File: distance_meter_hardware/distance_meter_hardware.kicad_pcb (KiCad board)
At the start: 2 copper layers, 62.2 x 53.3 mm, 6 parts, among them J1 PPPC071LFBN-RC, J2 PPPC071LFBN-RC, J3 PPPC141LFBN-RC, J4 PPPC141LFBN-RC, J5 PPPC071LFBN-RC, J6 PPPC071LFBN-RC

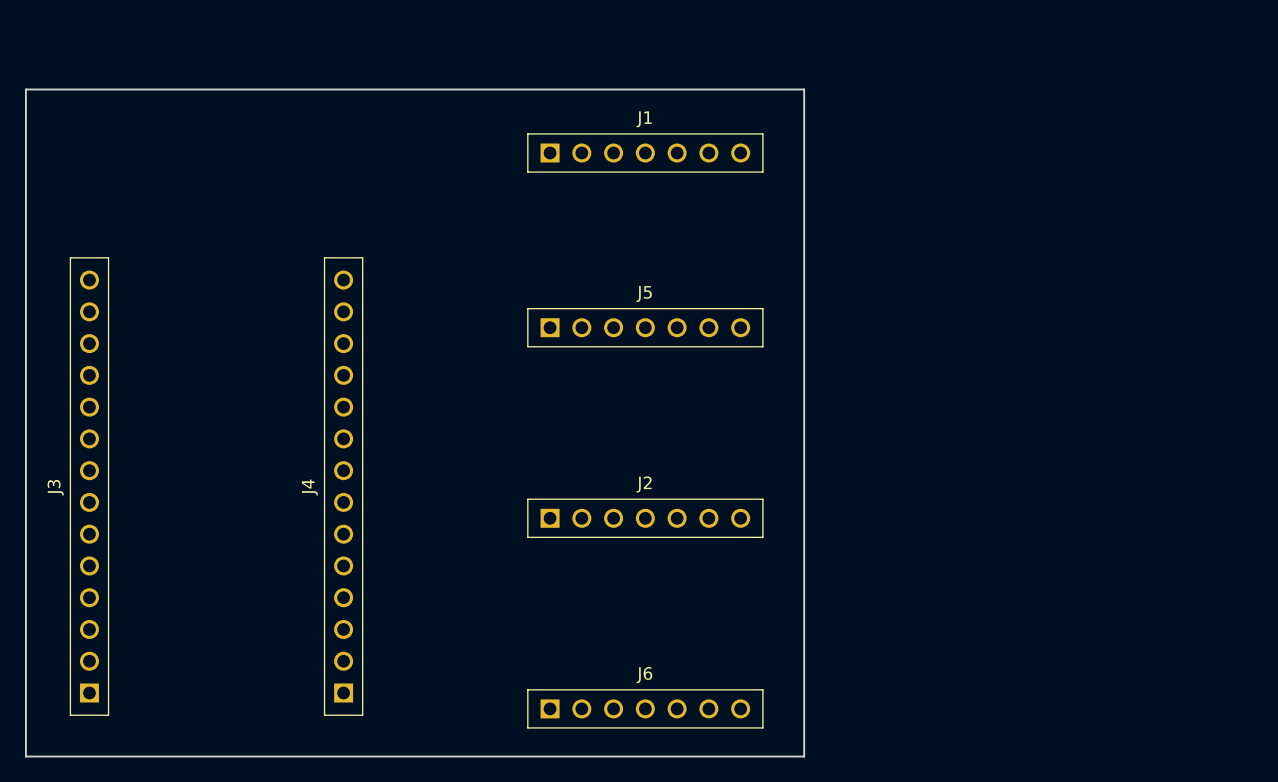
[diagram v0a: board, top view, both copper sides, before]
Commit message: Organize components and silk in layout
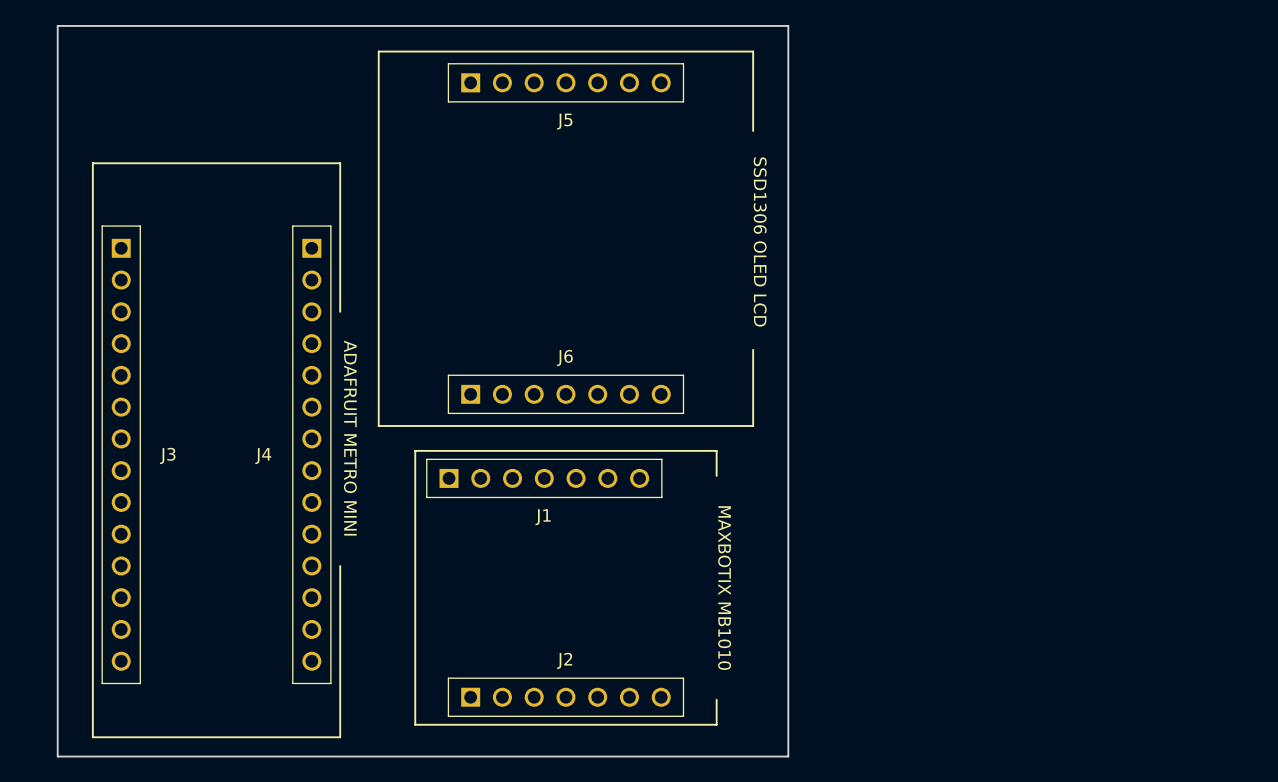
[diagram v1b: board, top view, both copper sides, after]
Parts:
- moved J1 27.2 mm to (97.3, 74.3)
- moved J6 25.9 mm to (99.1, 67.6)
- moved J5 20.6 mm to (99.1, 42.6)
- moved J2 15.7 mm to (99.1, 91.8)
- moved J4 3.59 mm to (78.7, 72.4), turned to 270 degrees
- moved J3 3.59 mm to (63.5, 72.4), turned to 270 degrees
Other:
- board size 62.2 x 53.3 mm -> 58.4 x 58.4 mm
- board text added: "ADAFRUIT METRO MINI"
- board text added: "MAXBOTIX MB1010"
- board text added: "SSD1306 OLED LCD"

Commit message: Resize layout to fit in project box
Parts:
- moved J5 34.6 mm to (130.8, 56.3)
- moved J6 34.6 mm to (130.8, 81.2)
- moved J4 31.5 mm to (110.0, 68.8)
- moved J3 31.5 mm to (94.8, 68.8)
- moved J1 26.4 mm to (75.1, 60.0)
- moved J2 26.4 mm to (76.9, 77.5)
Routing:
- net (no net): vias 0 -> 4
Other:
- board size 58.4 x 58.4 mm -> 95.5 x 55.5 mm
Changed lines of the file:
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@@
   (general
     (thickness 1.6)
-    (drawings 25)
-    (tracks 0)
+    (drawings 27)
+    (tracks 4)
     (zones 0)
     (modules 6)
@@
     (solder_mask_min_width 0.25)
     (aux_axis_origin 0 0)
+    (grid_origin 58.42 96.52)
     (visible_elements FFFDFF7F)
     (pcbplotparams
@@
   )
   (module headers:PPPC071LFBN-RC (layer F.Cu)
-    (at 97.33 74.280005)
+    (at 75.14 60.020005)
     (descr "http://www.sullinscorp.com/drawings/78_P(N)PxCxxxLFBN-RC,_10492-H.pdf")
     (tags "header, 1x7, socket")
@@
   )
   (module headers:PPPC071LFBN-RC (layer F.Cu)
-    (at 99.06 91.780005)
+    (at 76.87 77.520005)
     (descr "http://www.sullinscorp.com/drawings/78_P(N)PxCxxxLFBN-RC,_10492-H.pdf")
     (tags "header, 1x7, socket")
@@
   )
   (module headers:PPPC141LFBN-RC (layer F.Cu)
-    (at 63.5 72.39 270)
+    (at 94.77 68.77 270)
     (descr "http://www.sullinscorp.com/drawings/78_P(N)PxCxxxLFBN-RC,_10492-H.pdf")
     (tags "header, 1x14, socket")
@@
   )
   (module headers:PPPC141LFBN-RC (layer F.Cu)
-    (at 78.74 72.39 270)
+    (at 110.01 68.77 270)
     (descr "http://www.sullinscorp.com/drawings/78_P(N)PxCxxxLFBN-RC,_10492-H.pdf")
     (tags "header, 1x14, socket")
@@
   )
   (module headers:PPPC071LFBN-RC (layer F.Cu)
-    (at 99.06 42.648)
+    (at 130.83 56.3)
     (descr "http://www.sullinscorp.com/drawings/78_P(N)PxCxxxLFBN-RC,_10492-H.pdf")
     (tags "header, 1x7, socket")
@@
   )
   (module headers:PPPC071LFBN-RC (layer F.Cu)
-    (at 99.06 67.558)
+    (at 130.83 81.21)
     (descr "http://www.sullinscorp.com/drawings/78_P(N)PxCxxxLFBN-RC,_10492-H.pdf")
     (tags "header, 1x7, socket")
@@
     )
   )
-  (gr_poly (pts (xy 62.23 50.8) (xy 80.01 50.8) (xy 80.01 93.98) (xy 62.23 93.98)) (layer F.Fab) (width 0.1))
-  (gr_text "SSD1306 OLED LCD" (at 114.554 55.372 270) (layer F.SilkS)
+  (dimension 55.5 (width 0.15) (layer F.SilkS)
+    (gr_text "55.500 mm" (at 40.12 68.77 90) (layer F.SilkS)
+      (effects (font (size 1 1) (thickness 0.15)))
+    )
+    (feature1 (pts (xy 58.42 41.02) (xy 40.833579 41.02)))
+    (feature2 (pts (xy 58.42 96.52) (xy 40.833579 96.52)))
+    (crossbar (pts (xy 41.42 96.52) (xy 41.42 41.02)))
+    (arrow1a (pts (xy 41.42 41.02) (xy 42.006421 42.146504)))
+    (arrow1b (pts (xy 41.42 41.02) (xy 40.833579 42.146504)))
+    (arrow2a (pts (xy 41.42 96.52) (xy 42.006421 95.393496)))
+    (arrow2b (pts (xy 41.42 96.52) (xy 40.833579 95.393496)))
+  )
+  (dimension 95.5 (width 0.15) (layer F.SilkS)
+    (gr_text "95.500 mm" (at 106.17 103.32) (layer F.SilkS)
+      (effects (font (size 1 1) (thickness 0.15)))
+    )
+    (feature1 (pts (xy 153.92 96.52) (xy 153.92 102.606421)))
+    (feature2 (pts (xy 58.42 96.52) (xy 58.42 102.606421)))
+    (crossbar (pts (xy 58.42 102.02) (xy 153.92 102.02)))
+    (arrow1a (pts (xy 153.92 102.02) (xy 152.793496 102.606421)))
+    (arrow1b (pts (xy 153.92 102.02) (xy 152.793496 101.433579)))
+    (arrow2a (pts (xy 58.42 102.02) (xy 59.546504 102.606421)))
+    (arrow2b (pts (xy 58.42 102.02) (xy 59.546504 101.433579)))
+  )
+  (gr_poly (pts (xy 93.5 47.18) (xy 111.28 47.18) (xy 111.28 90.36) (xy 93.5 90.36)) (layer F.Fab) (width 0.1))
+  (gr_text "SSD1306 OLED LCD" (at 146.324 69.024 270) (layer F.SilkS)
     (effects (font (size 1 1) (thickness 0.15)))
   )
-  (gr_line (start 114.03 70.088) (end 114.03 64) (layer F.SilkS) (width 0.15))
-  (gr_line (start 84.09 70.088) (end 114.03 70.088) (layer F.SilkS) (width 0.15))
-  (gr_line (start 84.09 40.148) (end 84.09 70.088) (layer F.SilkS) (width 0.15))
-  (gr_line (start 114.03 40.148) (end 114.03 46.5) (layer F.SilkS) (width 0.15))
-  (gr_line (start 84.09 40.148) (end 114.03 40.148) (layer F.SilkS) (width 0.15))
-  (gr_poly (pts (xy 85.09 41.148) (xy 113.03 41.148) (xy 113.03 69.088) (xy 85.09 69.088)) (layer F.Fab) (width 0.1))
-  (gr_poly (pts (xy 88.01 73.080005) (xy 110.11 73.080005) (xy 110.11 92.980005) (xy 88.01 92.980005)) (layer F.Fab) (width 0.1))
-  (gr_line (start 111.11 93.980005) (end 111.11 91.980005) (layer F.SilkS) (width 0.15))
-  (gr_line (start 111.11 72.080005) (end 111.11 74.080005) (layer F.SilkS) (width 0.15))
-  (gr_text "MAXBOTIX MB1010" (at 111.71 83.030005 270) (layer F.SilkS)
+  (gr_line (start 145.8 83.74) (end 145.8 77.652) (layer F.SilkS) (width 0.15))
+  (gr_line (start 115.86 83.74) (end 145.8 83.74) (layer F.SilkS) (width 0.15))
+  (gr_line (start 115.86 53.8) (end 115.86 83.74) (layer F.SilkS) (width 0.15))
+  (gr_line (start 145.8 53.8) (end 145.8 60.152) (layer F.SilkS) (width 0.15))
+  (gr_line (start 115.86 53.8) (end 145.8 53.8) (layer F.SilkS) (width 0.15))
+  (gr_poly (pts (xy 116.86 54.8) (xy 144.8 54.8) (xy 144.8 82.74) (xy 116.86 82.74)) (layer F.Fab) (width 0.1))
+  (gr_poly (pts (xy 65.82 58.820005) (xy 87.92 58.820005) (xy 87.92 78.720005) (xy 65.82 78.720005)) (layer F.Fab) (width 0.1))
+  (gr_line (start 88.92 79.720005) (end 88.92 77.720005) (layer F.SilkS) (width 0.15))
+  (gr_line (start 88.92 57.820005) (end 88.92 59.820005) (layer F.SilkS) (width 0.15))
+  (gr_text "MAXBOTIX MB1010" (at 89.52 68.770005 270) (layer F.SilkS)
     (effects (font (size 1 1) (thickness 0.15)))
   )
-  (gr_line (start 87.01 93.980005) (end 87.01 72.080005) (layer F.SilkS) (width 0.15))
-  (gr_line (start 111.11 93.980005) (end 87.01 93.980005) (layer F.SilkS) (width 0.15))
-  (gr_line (start 87.01 72.080005) (end 111.11 72.080005) (layer F.SilkS) (width 0.15))
-  (gr_line (start 81.01 94.98) (end 81.01 81.28) (layer F.SilkS) (width 0.15))
-  (gr_line (start 81.01 49.08) (end 81.01 60.96) (layer F.SilkS) (width 0.15))
-  (gr_text "ADAFRUIT METRO MINI" (at 81.788 71.12 270) (layer F.SilkS)
+  (gr_line (start 64.82 79.720005) (end 64.82 57.820005) (layer F.SilkS) (width 0.15))
+  (gr_line (start 88.92 79.720005) (end 64.82 79.720005) (layer F.SilkS) (width 0.15))
+  (gr_line (start 64.82 57.820005) (end 88.92 57.820005) (layer F.SilkS) (width 0.15))
+  (gr_line (start 112.28 91.36) (end 112.28 77.66) (layer F.SilkS) (width 0.15))
+  (gr_line (start 112.28 45.46) (end 112.28 57.34) (layer F.SilkS) (width 0.15))
+  (gr_text "ADAFRUIT METRO MINI" (at 113.058 67.5 270) (layer F.SilkS)
     (effects (font (size 1 1) (thickness 0.15)))
   )
-  (gr_line (start 61.23 94.98) (end 81.01 94.98) (layer F.SilkS) (width 0.15))
-  (gr_line (start 61.23 49.08) (end 61.23 94.98) (layer F.SilkS) (width 0.15))
-  (gr_line (start 61.23 49.08) (end 81.01 49.08) (layer F.SilkS) (width 0.15))
-  (gr_line (start 58.42 96.52) (end 58.42 38.1) (layer Edge.Cuts) (width 0.15))
-  (gr_line (start 116.84 96.52) (end 58.42 96.52) (layer Edge.Cuts) (width 0.15))
-  (gr_line (start 116.84 38.1) (end 116.84 96.52) (layer Edge.Cuts) (width 0.15))
-  (gr_line (start 58.42 38.1) (end 116.84 38.1) (layer Edge.Cuts) (width 0.15))
+  (gr_line (start 92.5 91.36) (end 112.28 91.36) (layer F.SilkS) (width 0.15))
+  (gr_line (start 92.5 45.46) (end 92.5 91.36) (layer F.SilkS) (width 0.15))
+  (gr_line (start 92.5 45.46) (end 112.28 45.46) (layer F.SilkS) (width 0.15))
+  (gr_line (start 58.42 96.52) (end 58.42 41.02) (layer Edge.Cuts) (width 0.15))
+  (gr_line (start 153.92 96.52) (end 58.42 96.52) (layer Edge.Cuts) (width 0.15))
+  (gr_line (start 153.92 41.02) (end 153.92 96.52) (layer Edge.Cuts) (width 0.15))
+  (gr_line (start 58.42 41.02) (end 153.92 41.02) (layer Edge.Cuts) (width 0.15))
+  (via (at 150.17 44.77) (size 5.4) (drill 2.85) (layers F.Cu B.Cu) (net 0))
+  (via (at 150.17 92.77) (size 5.4) (drill 2.85) (layers F.Cu B.Cu) (net 0))
+  (via (at 62.17 92.77) (size 5.4) (drill 2.85) (layers F.Cu B.Cu) (net 0))
+  (via (at 62.17 44.77) (size 5.4) (drill 2.85) (layers F.Cu B.Cu) (net 0))
 )

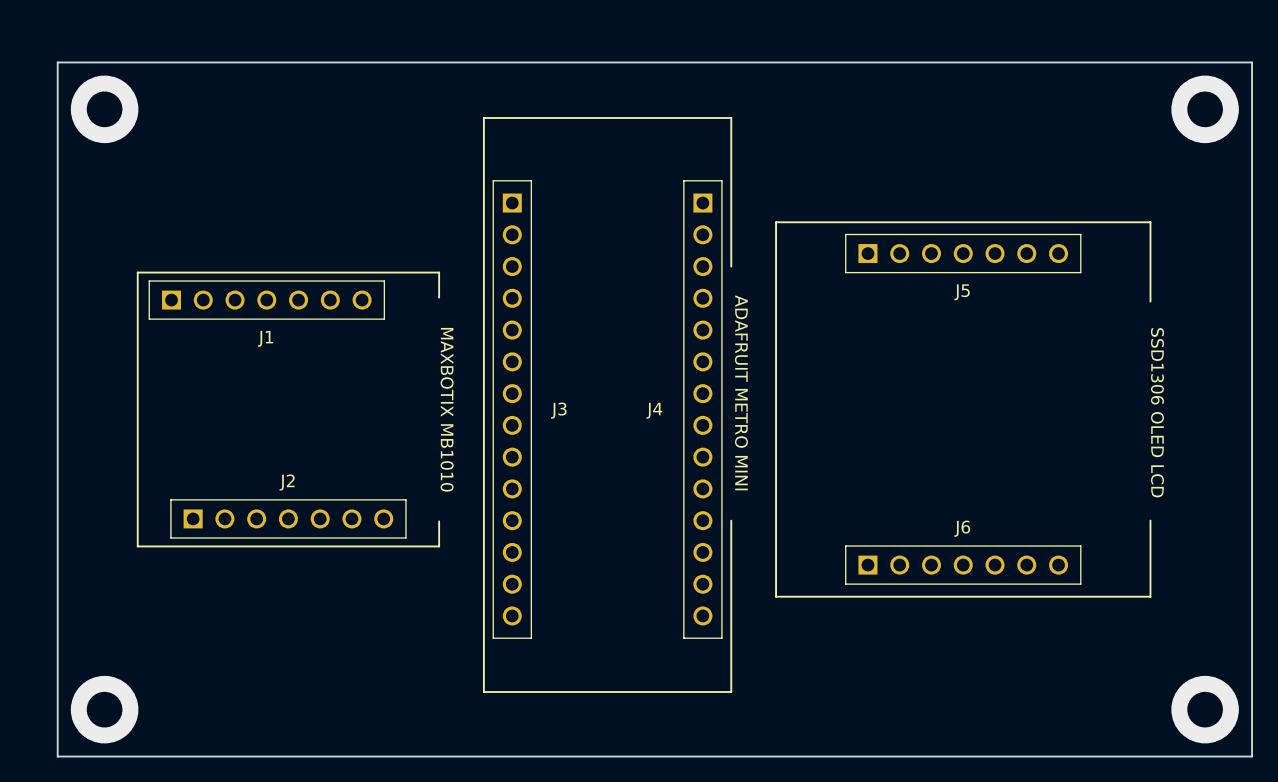
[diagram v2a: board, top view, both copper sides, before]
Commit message: Add routes to schematic. Update netlist
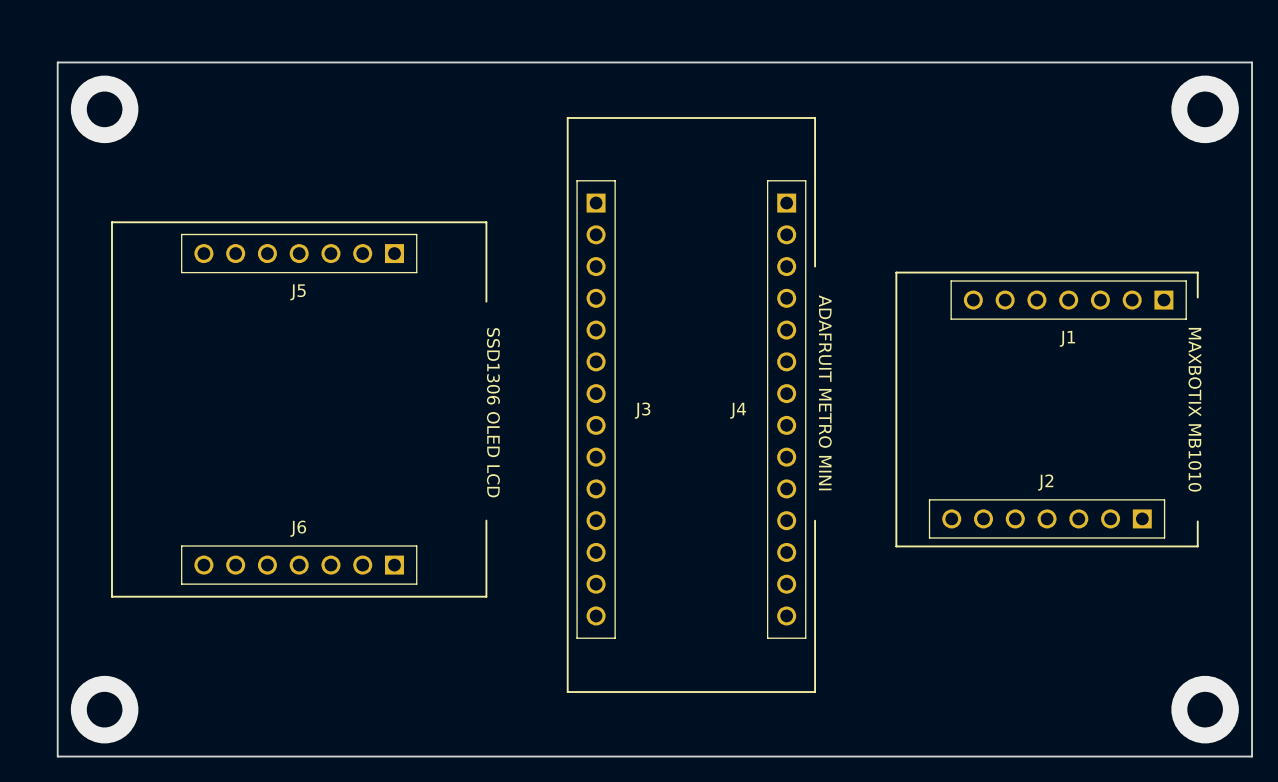
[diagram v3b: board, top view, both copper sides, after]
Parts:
- moved J1 64.1 mm to (139.3, 60.0), turned to 180 degrees
- moved J2 60.7 mm to (137.5, 77.5), turned to 180 degrees
- moved J5 53.1 mm to (77.7, 56.3), turned to 180 degrees
- moved J6 53.1 mm to (77.7, 81.2), turned to 180 degrees
- moved J3 6.70 mm to (101.5, 68.8)
- moved J4 6.70 mm to (116.7, 68.8)
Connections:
- J1 pad 6: Net-(J1-Pad6) -> +5V
- J1 pad 7: Net-(J1-Pad7) -> GND
- J4 pad 6: Net-(J4-Pad6) -> Net-(J1-Pad3)
- J5 pad 1: Net-(J5-Pad1) -> Net-(J3-Pad2)
- J5 pad 2: Net-(J5-Pad2) -> Net-(J3-Pad3)
- J5 pad 3: Net-(J5-Pad3) -> Net-(J3-Pad6)
- J5 pad 4: Net-(J5-Pad4) -> Net-(J3-Pad5)
- J5 pad 5: Net-(J5-Pad5) -> Net-(J3-Pad4)
- J5 pad 6: Net-(J5-Pad6) -> +5V
- J5 pad 7: Net-(J5-Pad7) -> GND
